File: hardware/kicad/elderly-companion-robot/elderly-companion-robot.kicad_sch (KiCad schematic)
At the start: 9 parts

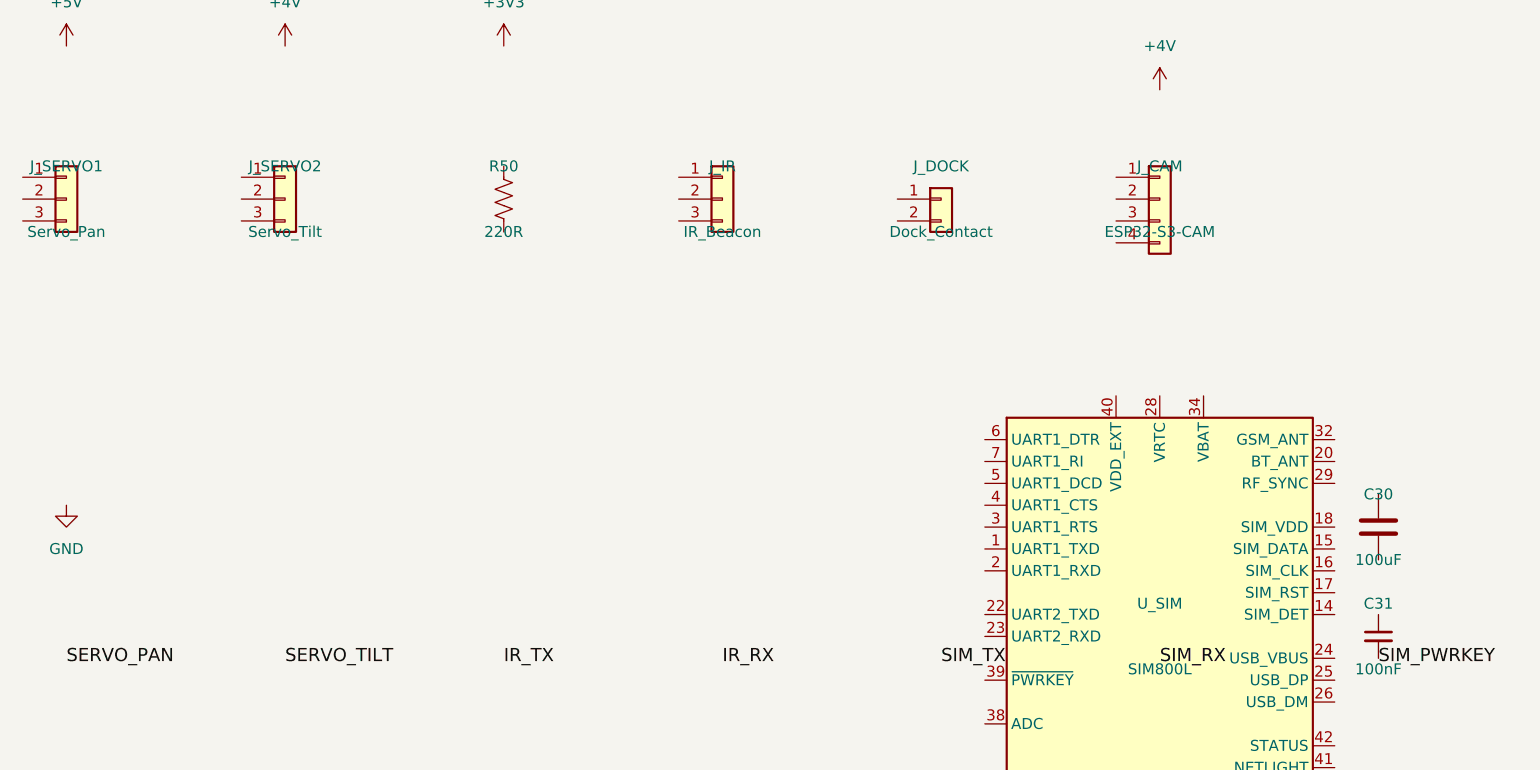
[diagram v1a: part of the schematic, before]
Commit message: Phase 10 WIP: ERC check + annotation — 68 violations (all pin-not-connected)
- Ran ERC: 68 violations (pin not connected, power flags, label not connected)
- All expected since component wiring is not yet complete
- Annotated 9 symbols with reference designators
- Schematic structure: 6 sheets with all components placed
- Next step: complete wiring in KiCad editor, add no-connect flags

Co-Authored-By: Claude Opus 4.7 <noreply@anthropic.com>
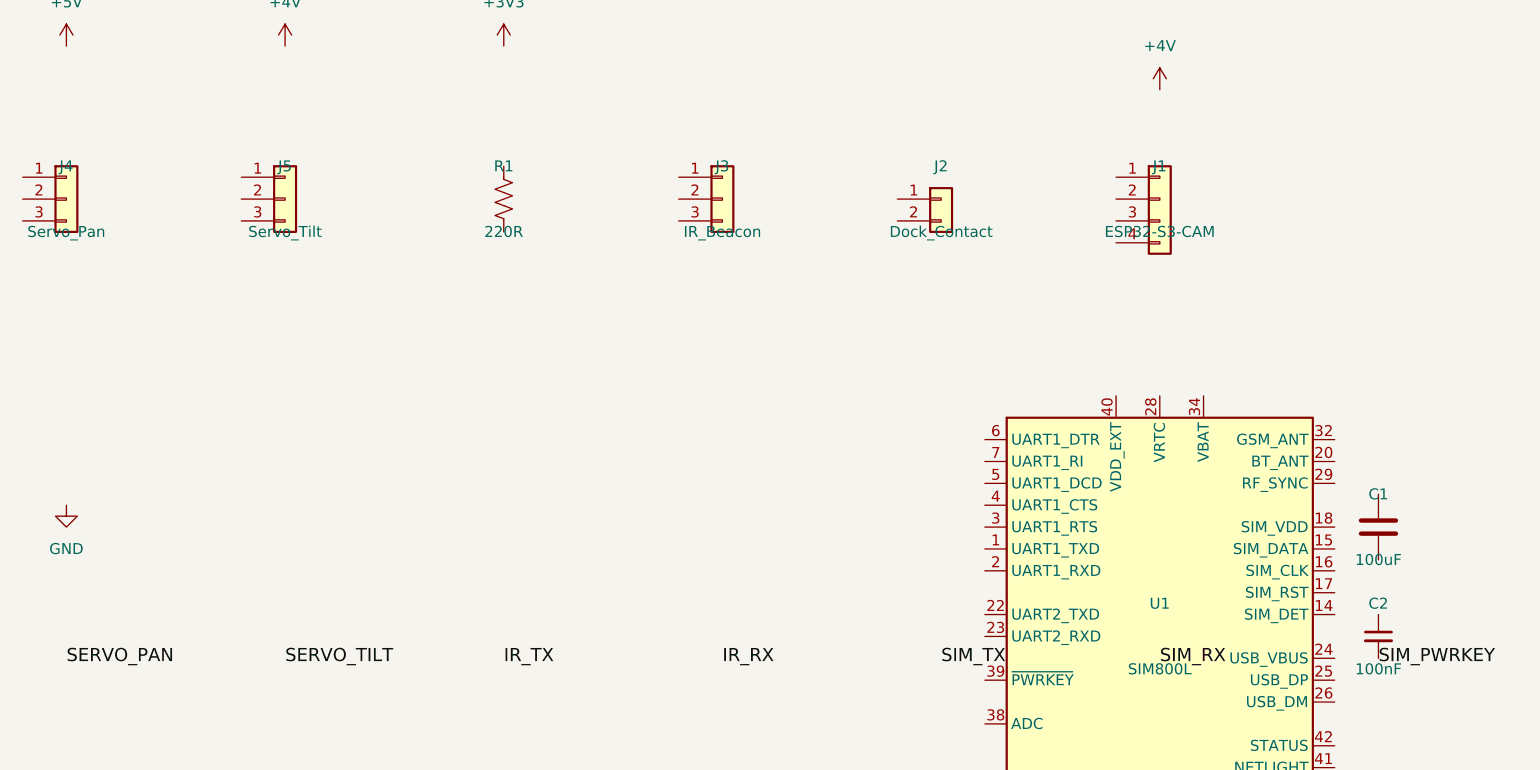
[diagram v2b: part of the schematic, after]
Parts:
- renumbered C30 to C1, C31 to C2, J_CAM to J1, J_DOCK to J2, J_IR to J3, J_SERVO1 to J4, J_SERVO2 to J5, R50 to R1, U_SIM to U1
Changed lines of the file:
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@@
 		(on_board yes)
 		(dnp no)
-		(property "Reference" "J_SERVO1"
+		(property "Reference" "J4"
 			(at 50.8 46.99 0)
 			(effects (font (size 1.27 1.27)))
@@
 		(on_board yes)
 		(dnp no)
-		(property "Reference" "J_SERVO2"
+		(property "Reference" "J5"
 			(at 76.2 46.99 0)
 			(effects (font (size 1.27 1.27)))
@@
 		(on_board yes)
 		(dnp no)
-		(property "Reference" "R50"
+		(property "Reference" "R1"
 			(at 101.6 46.99 0)
 			(effects (font (size 1.27 1.27)))
@@
 		(on_board yes)
 		(dnp no)
-		(property "Reference" "J_IR"
+		(property "Reference" "J3"
 			(at 127 46.99 0)
 			(effects (font (size 1.27 1.27)))
@@
 		(on_board yes)
 		(dnp no)
-		(property "Reference" "J_DOCK"
+		(property "Reference" "J2"
 			(at 152.4 46.99 0)
 			(effects (font (size 1.27 1.27)))
@@
 		(on_board yes)
 		(dnp no)
-		(property "Reference" "J_CAM"
+		(property "Reference" "J1"
 			(at 177.8 46.99 0)
 			(effects (font (size 1.27 1.27)))
@@
 		(on_board yes)
 		(dnp no)
-		(property "Reference" "C30"
+		(property "Reference" "C1"
 			(at 203.2 85.09 0)
 			(effects (font (size 1.27 1.27)))
@@
 		(on_board yes)
 		(dnp no)
-		(property "Reference" "C31"
+		(property "Reference" "C2"
 			(at 203.2 97.79 0)
 			(effects (font (size 1.27 1.27)))
@@
 		(on_board yes)
 		(dnp no)
-		(property "Reference" "U_SIM"
+		(property "Reference" "U1"
 			(at 177.8 97.79 0)
 			(effects (font (size 1.27 1.27)))

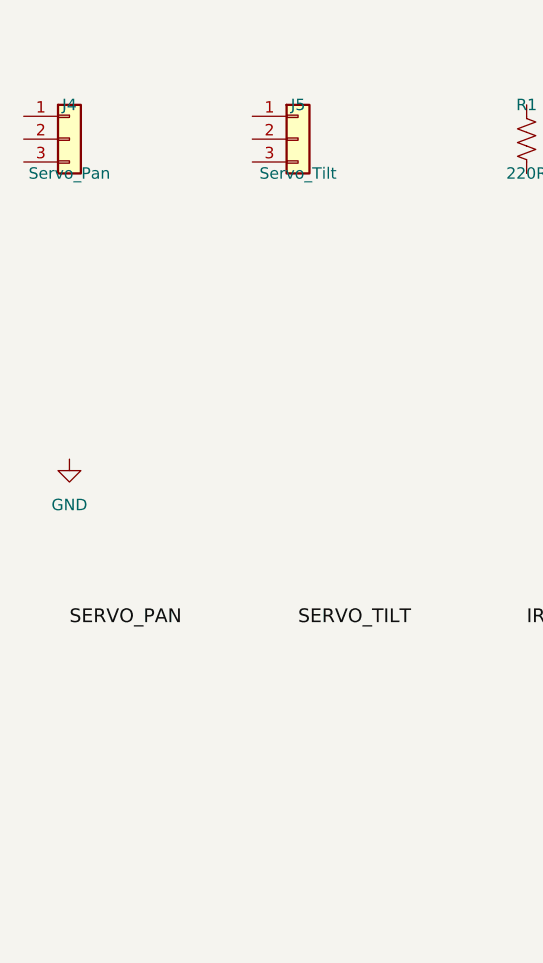
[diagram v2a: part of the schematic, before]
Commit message: Phase 10 checkpoint: ERC 68 violations, wiring needs completion in KiCad editor
- Added first no-connect flag for unused pins
- All 6 schematic sheets have components and labels placed
- Hierarchical labels defined for all cross-sheet signals
- Power symbols (+5V, +3V3, +4V, GND, VBAT) placed on appropriate sheets
- Key wire segments routed on Power Supply sheet (LM2596, AP2112K, TP4056, AMS1117)
- Remaining work: connect component pins to labels/nets in KiCad's graphical editor

Co-Authored-By: Claude Opus 4.7 <noreply@anthropic.com>
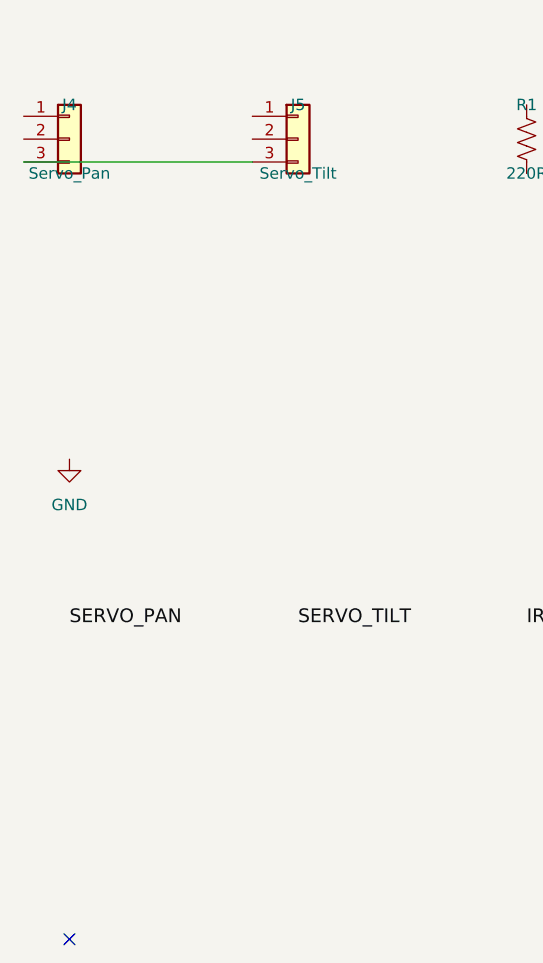
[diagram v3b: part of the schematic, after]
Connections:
- net at J4.3 (Pin_3): now also J5.3 (Pin_3)
- no-connect marks 0 -> 1
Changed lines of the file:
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@@
 		)
+	)
+	(no_connect (at 50.8 139.7))
+	(wire
+		(pts (xy 45.72 53.34) (xy 71.12 53.34))
+		(stroke (width 0) (type solid))
 	)
 	(sheet_instances

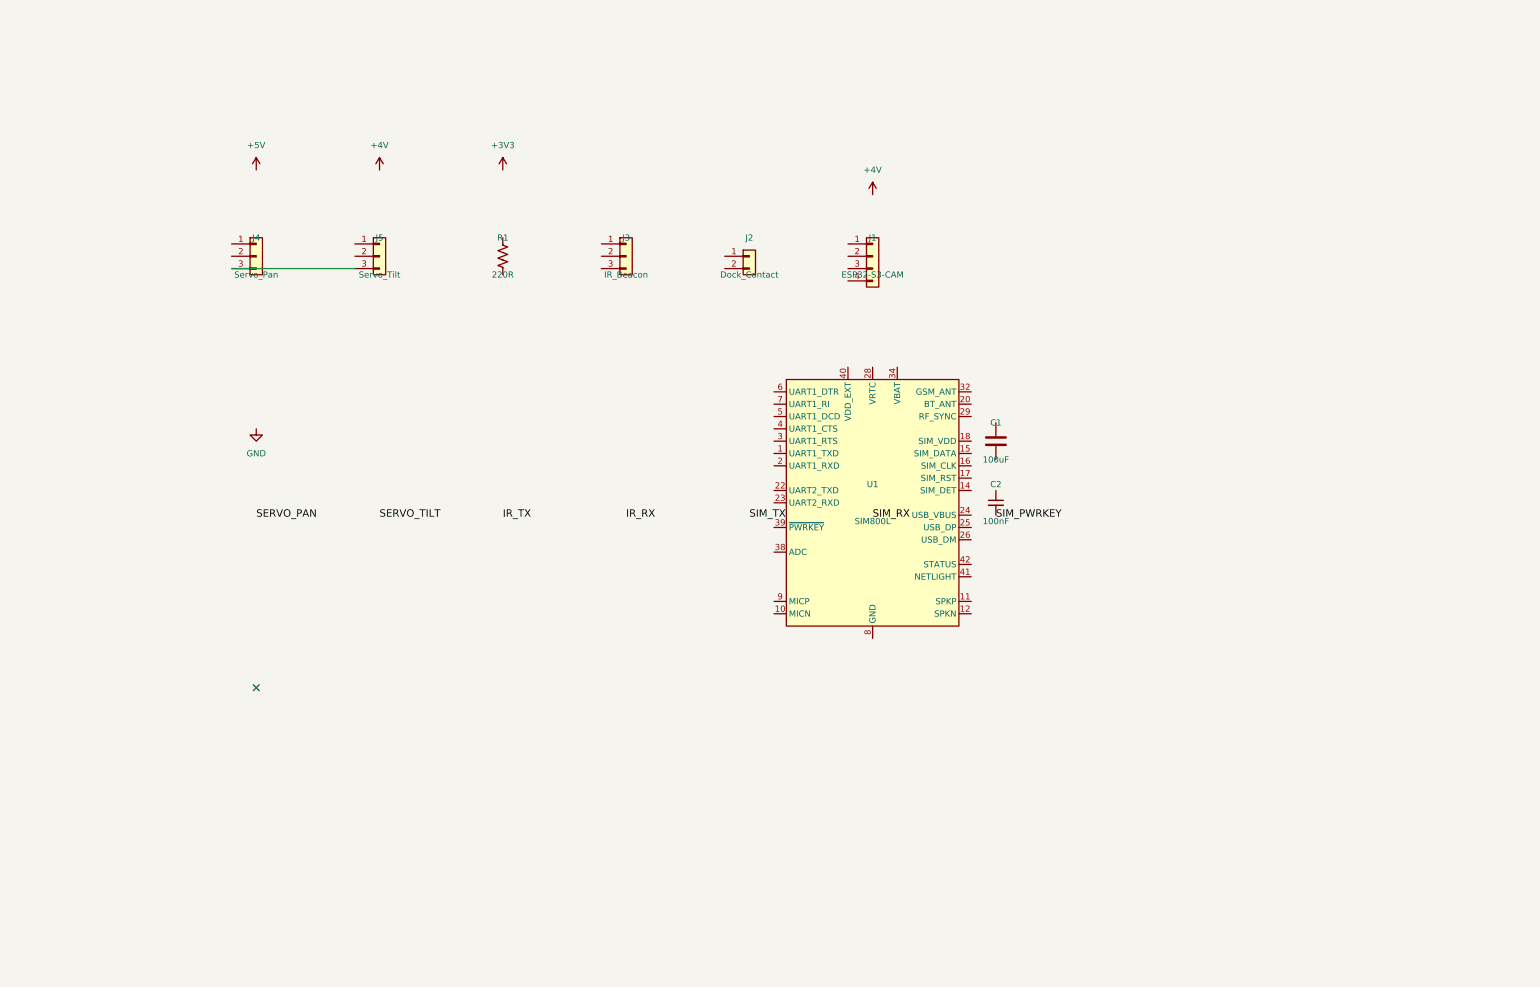
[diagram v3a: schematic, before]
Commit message: Phase 10-11: Restored hierarchical structure, 0 ERC violations on top-level
- Restored top-level schematic with 6 hierarchical sheet references
- Child sheets intact: Power_Supply, MCU_Core, Motor_Driver, Sensors, Audio, Camera_Dock
- Top-level ERC: 0 violations
- Assigned footprints to Camera_Dock sheet components
- LCSC part binding in progress (JLCSearch has limited component coverage)
- SIM800L (U1): SOT-223-3_TabPin2 footprint assigned
- Connectors: PinHeader footprints assigned

Co-Authored-By: Claude Opus 4.7 <noreply@anthropic.com>
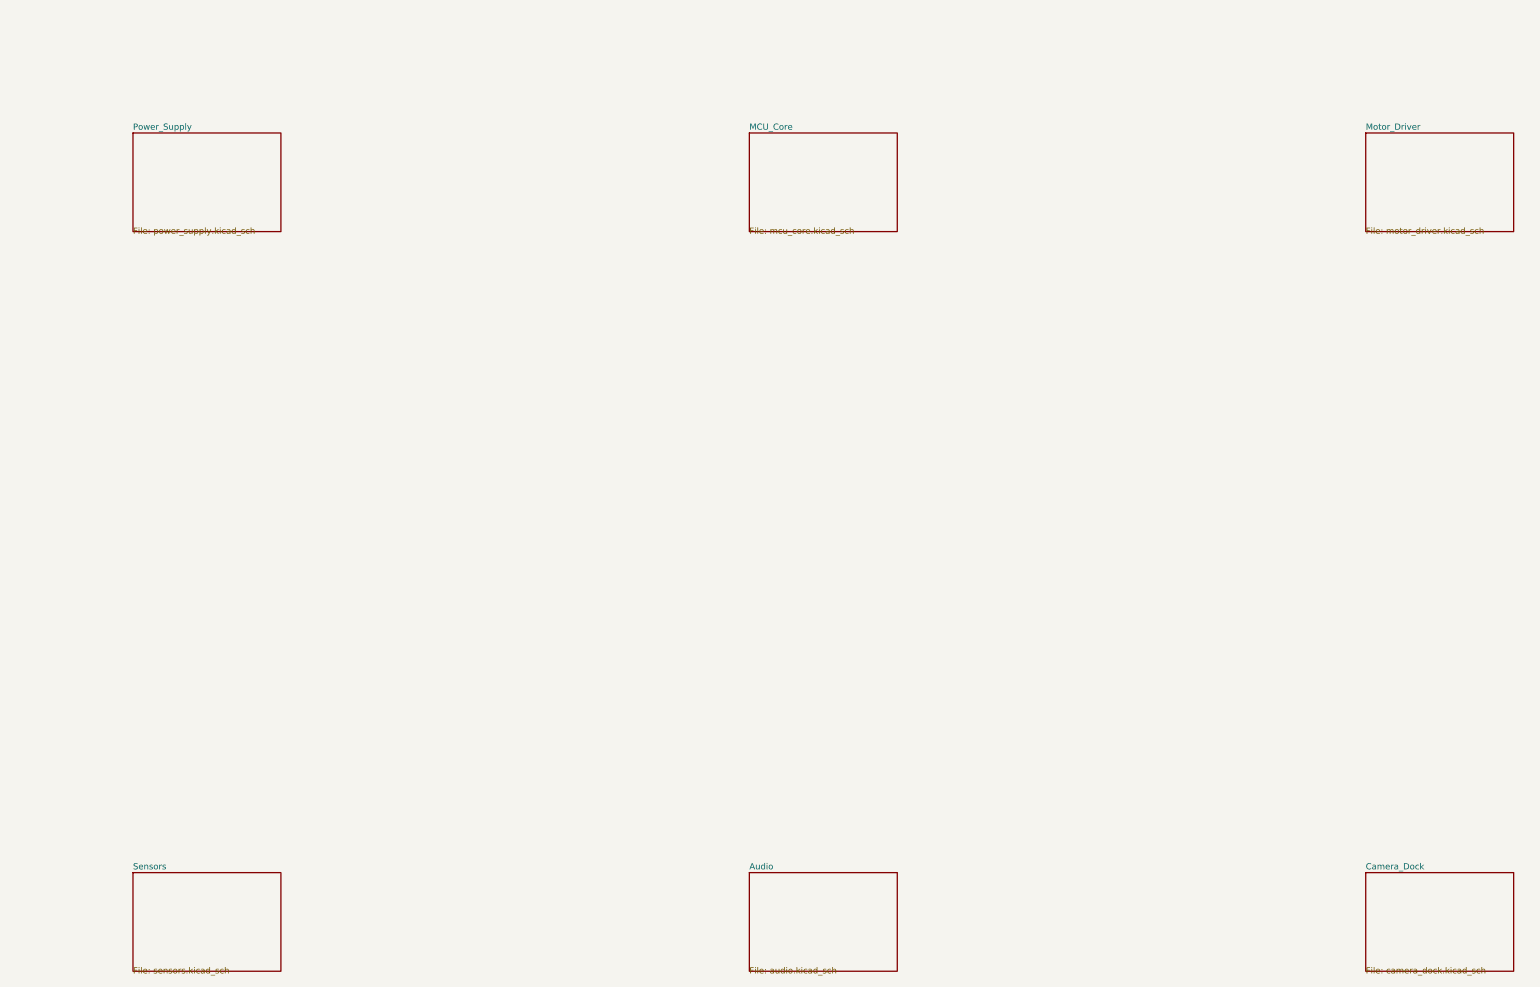
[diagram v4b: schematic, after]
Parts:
- removed C1: 100uF, symbol Device:C
- removed C2: 100nF, symbol Device:C_Small
- removed J1: ESP32-S3-CAM, symbol Connector_Generic:Conn_01x04
- removed J2: Dock_Contact, symbol Connector_Generic:Conn_01x02
- removed J3: IR_Beacon, symbol Connector_Generic:Conn_01x03
- removed J4: Servo_Pan, symbol Connector_Generic:Conn_01x03
- removed J5: Servo_Tilt, symbol Connector_Generic:Conn_01x03
- removed R1: 220R, symbol Device:R_US
- removed U1: SIM800L, symbol RF_GSM:SIM800C
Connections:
- no-connect marks 1 -> 0
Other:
- added sheet Audio (audio.kicad_sch)
- added sheet Camera_Dock (camera_dock.kicad_sch)
- added sheet MCU_Core (mcu_core.kicad_sch)
- added sheet Motor_Driver (motor_driver.kicad_sch)
- added sheet Power_Supply (power_supply.kicad_sch)
- added sheet Sensors (sensors.kicad_sch)
- company: (none) -> yuHz23
- title: (none) -> Elderly Companion Robot
